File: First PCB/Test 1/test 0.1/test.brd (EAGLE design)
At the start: 62.2 x 39 mm, 7 parts, among them SW2 B3U-1000P

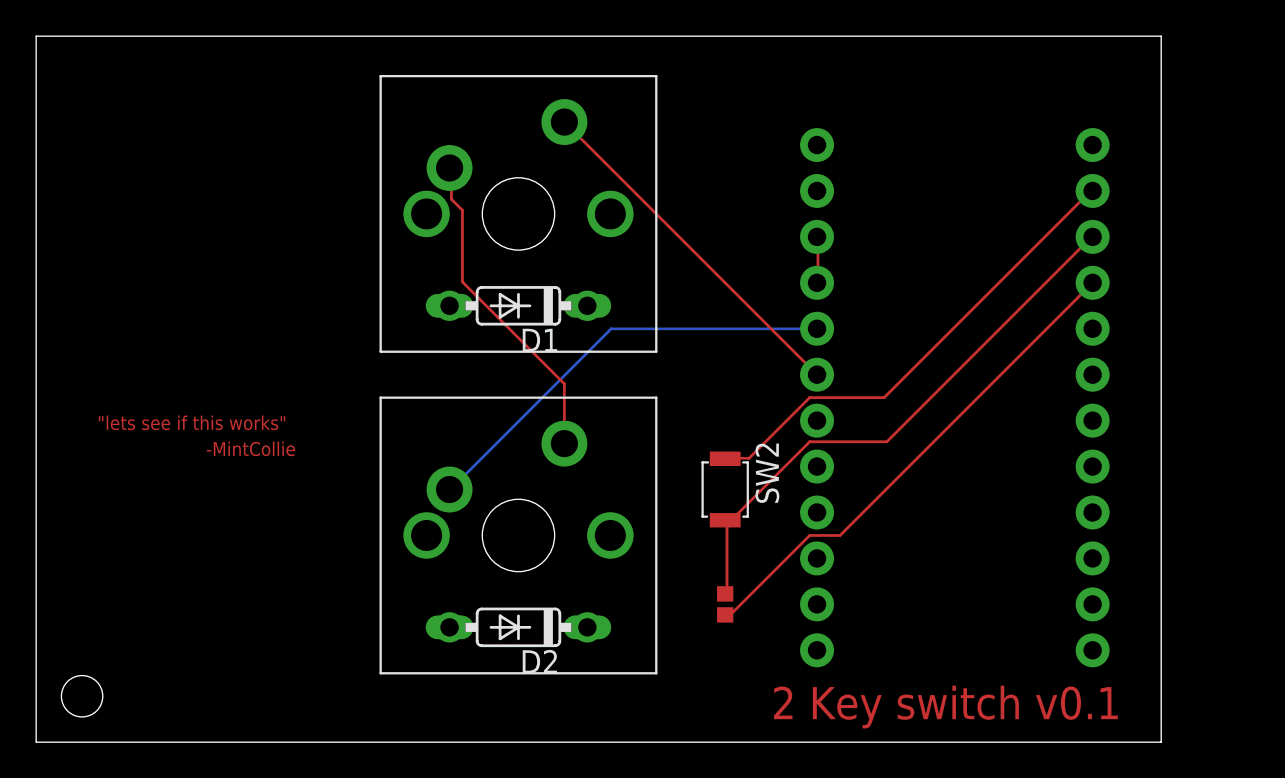
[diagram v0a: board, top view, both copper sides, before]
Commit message: Added QR code to bottom layer, Need to resize. Need to fix diode route and then submit for review
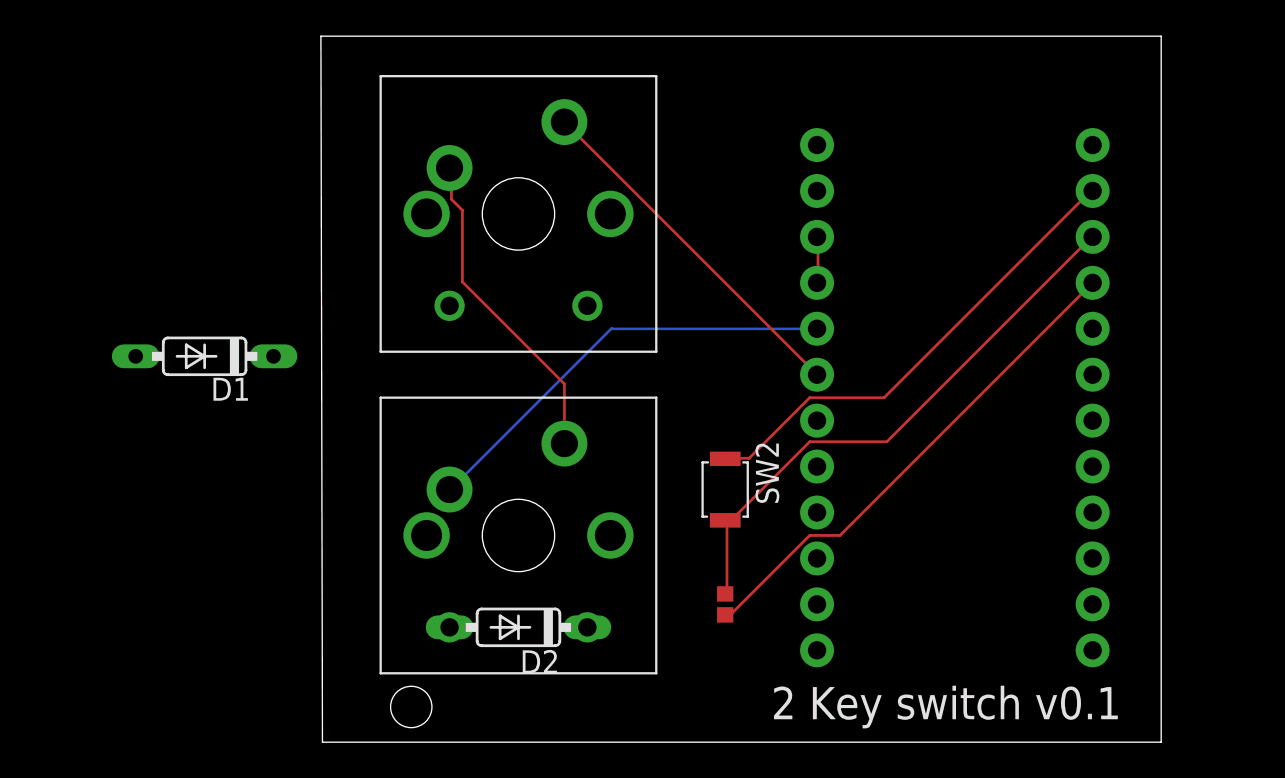
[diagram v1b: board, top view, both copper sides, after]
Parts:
- moved D1 17.6 mm to (71.5, 44.2)
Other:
- board size 62.2 x 39 mm -> 46.5 x 39 mm
- board text added: "C:/Users/Mint/Pictures/test2.bmp"

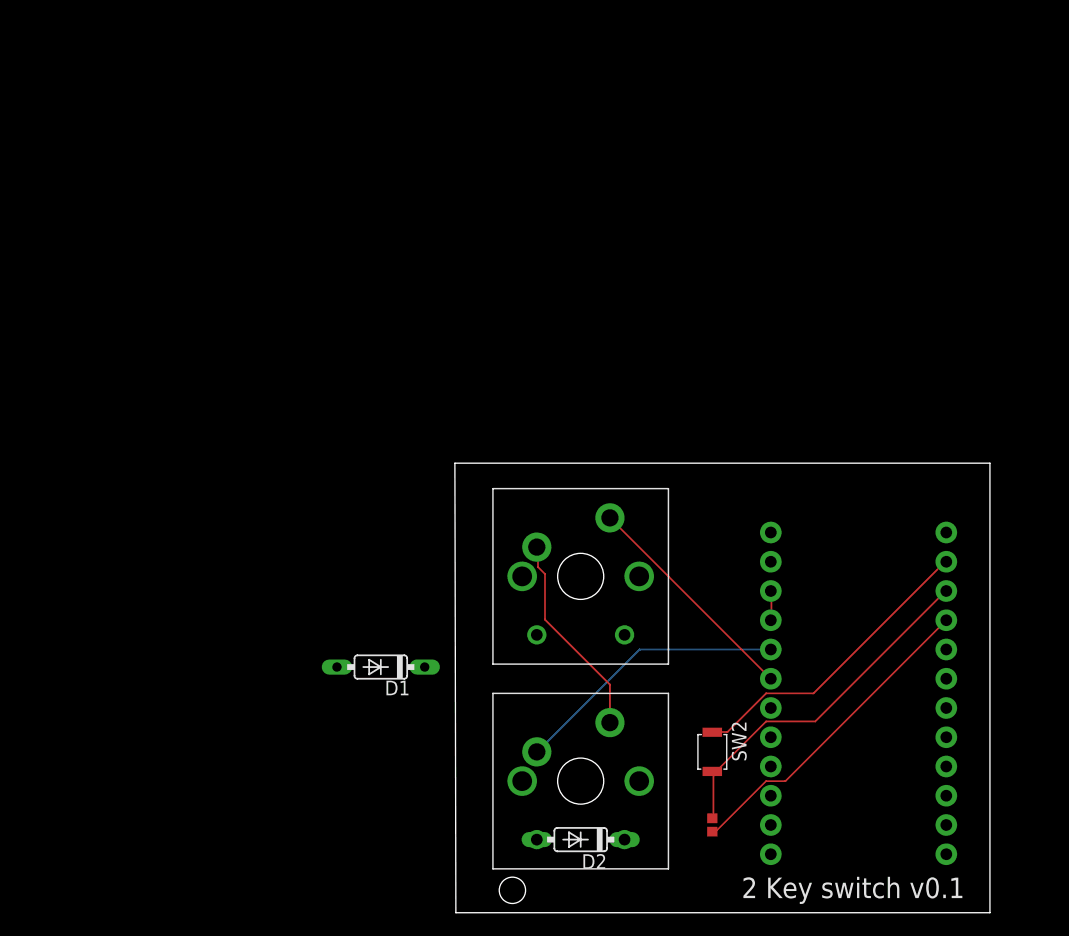
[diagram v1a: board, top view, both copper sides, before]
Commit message: slight changes to board layout need to finish still
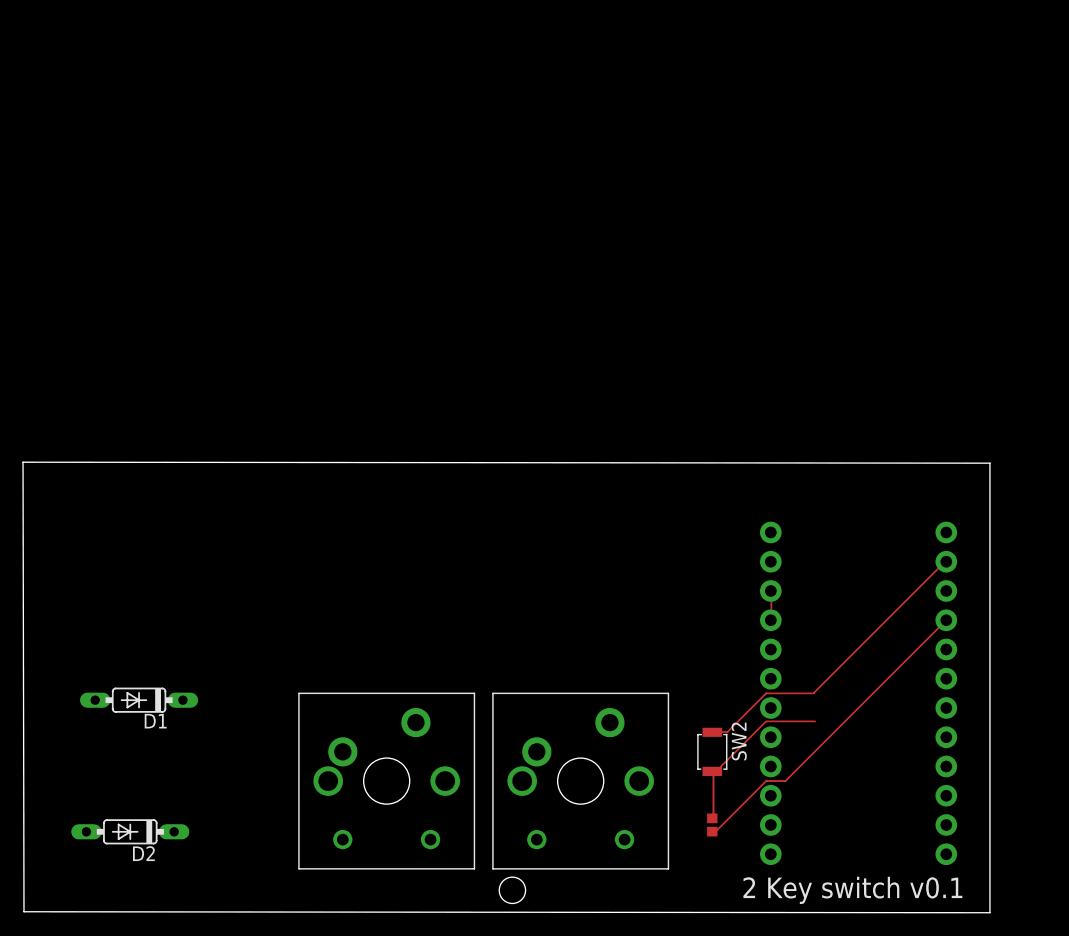
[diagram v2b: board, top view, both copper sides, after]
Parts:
- moved D2 39.1 mm to (49.8, 29.9)
- moved DIODE1 24.5 mm to (72.1, 34.3)
- moved D1 21.2 mm to (50.5, 41.3)
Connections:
- removed net N$10: D1.C, DIODE1.D2
- removed net N$6: B1.6, DIODE1.SW2
- removed net N$8: D2.C, DIODE.D2
- removed net N$9: D1.A, DIODE1.D1
- net N$4: now also B1.6; no longer B1.5
- net N$5: now also D2.C; no longer DIODE.SW2
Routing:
- net N$4: track 24.0 -> 0.11 mm
- net N$6: track 19.8 -> 0.00 mm
- net N$5: track 17.9 -> 0.00 mm
- net N$1: track 31.0 -> 15.0 mm
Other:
- board size 46.5 x 39 mm -> 84 x 39.1 mm
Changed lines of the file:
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@@
 <board>
 <plain>
-<wire x1="78.06108125" y1="22.86" x2="124.44" y2="22.86" width="0" layer="20"/>
+<wire x1="40.5575" y1="22.944659375" x2="124.44" y2="22.86" width="0" layer="20"/>
 <wire x1="124.44" y1="22.86" x2="124.44" y2="61.9" width="0" layer="20"/>
-<wire x1="124.44" y1="61.9" x2="77.976421875" y2="61.900003125" width="0" layer="20"/>
-<wire x1="77.976421875" y1="61.900003125" x2="78.06108125" y2="22.86" width="0" layer="20"/>
+<wire x1="124.44" y1="61.9" x2="40.472840625" y2="61.9846625" width="0" layer="20"/>
+<wire x1="40.472840625" y1="61.9846625" x2="40.5575" y2="22.944659375" width="0" layer="20"/>
 <text x="102.87" y="24.13" size="1.778" layer="25" font="vector">2 Key switch v0.1</text>
 <hole x="82.971509375" y="24.8073875" drill="2.286"/>
@@
 <attribute name="VALUE" x="113.03" y="26.416" size="0.6096" layer="27" font="vector" ratio="20" align="top-center"/>
 </element>
-<element name="D1" library="diode" library_urn="urn:adsk.eagle:library:210" package="DO35-7" package3d_urn="urn:adsk.eagle:package:43339/2" value="1N4148DO35-7" x="71.54506875" y="44.196278125" smashed="yes" rot="R180">
-<attribute name="MF" value="" x="47.41506875" y="100.076278125" size="1.778" layer="27" rot="R180" display="off"/>
-<attribute name="MPN" value="" x="47.41506875" y="100.076278125" size="1.778" layer="27" rot="R180" display="off"/>
-<attribute name="NAME" x="74.08504375" y="43.010934375" size="1.27" layer="25" ratio="10" rot="R180"/>
-<attribute name="OC_NEWARK" value="unknown" x="47.41506875" y="100.076278125" size="1.778" layer="27" rot="R180" display="off"/>
+<element name="D1" library="diode" library_urn="urn:adsk.eagle:library:210" package="DO35-7" package3d_urn="urn:adsk.eagle:package:43339/2" value="1N4148DO35-7" x="50.5498375" y="41.3179" smashed="yes" rot="R180">
+<attribute name="MF" value="" x="26.4198375" y="97.1979" size="1.778" layer="27" rot="R180" display="off"/>
+<attribute name="MPN" value="" x="26.4198375" y="97.1979" size="1.778" layer="27" rot="R180" display="off"/>
+<attribute name="NAME" x="53.0898125" y="40.13255625" size="1.27" layer="25" ratio="10" rot="R180"/>
+<attribute name="OC_NEWARK" value="unknown" x="26.4198375" y="97.1979" size="1.778" layer="27" rot="R180" display="off"/>
 </element>
-<element name="D2" library="diode" library_urn="urn:adsk.eagle:library:210" package="DO35-7" package3d_urn="urn:adsk.eagle:package:43339/2" value="1N4148DO35-7" x="88.9" y="29.21" smashed="yes" rot="R180">
-<attribute name="MF" value="" x="48.26" y="85.09" size="1.778" layer="27" rot="R180" display="off"/>
-<attribute name="MPN" value="" x="48.26" y="85.09" size="1.778" layer="27" rot="R180" display="off"/>
-<attribute name="NAME" x="91.186" y="27.94" size="1.27" layer="25" ratio="10" rot="R180"/>
-<attribute name="OC_NEWARK" value="unknown" x="48.26" y="85.09" size="1.778" layer="27" rot="R180" display="off"/>
+<element name="D2" library="diode" library_urn="urn:adsk.eagle:library:210" package="DO35-7" package3d_urn="urn:adsk.eagle:package:43339/2" value="1N4148DO35-7" x="49.7879125" y="29.887265625" smashed="yes" rot="R180">
+<attribute name="MF" value="" x="9.1479125" y="85.767265625" size="1.778" layer="27" rot="R180" display="off"/>
+<attribute name="MPN" value="" x="9.1479125" y="85.767265625" size="1.778" layer="27" rot="R180" display="off"/>
+<attribute name="NAME" x="52.0739125" y="28.617265625" size="1.27" layer="25" ratio="10" rot="R180"/>
+<attribute name="OC_NEWARK" value="unknown" x="9.1479125" y="85.767265625" size="1.778" layer="27" rot="R180" display="off"/>
 </element>
 <element name="DIODE" library="cherrymx" package="CHERRY-MX-DIODE" value="CHERRY-MX-DIODE" x="88.9" y="34.29" smashed="yes">
@@
 <attribute name="OC_NEWARK" value="unknown" x="129.54" y="25.4" size="1.778" layer="27" display="off"/>
 </element>
-<element name="DIODE1" library="cherrymx" package="CHERRY-MX-DIODE" value="CHERRY-MX-DIODE" x="88.9" y="52.07" smashed="yes">
-<attribute name="MF" value="" x="110.49" y="7.62" size="1.778" layer="27" display="off"/>
-<attribute name="MPN" value="" x="110.49" y="7.62" size="1.778" layer="27" display="off"/>
-<attribute name="OC_NEWARK" value="unknown" x="110.49" y="7.62" size="1.778" layer="27" display="off"/>
+<element name="DIODE1" library="cherrymx" package="CHERRY-MX-DIODE" value="CHERRY-MX-DIODE" x="72.05301875" y="34.291778125" smashed="yes">
+<attribute name="MF" value="" x="93.64301875" y="-10.158221875" size="1.778" layer="27" display="off"/>
+<attribute name="MPN" value="" x="93.64301875" y="-10.158221875" size="1.778" layer="27" display="off"/>
+<attribute name="OC_NEWARK" value="unknown" x="93.64301875" y="-10.158221875" size="1.778" layer="27" display="off"/>
 </element>
 <element name="R1" library="SparkFun-Resistors" package="0402" value="10k" x="100.33" y="30.48" smashed="yes" rot="R90">
@@
 <wire x1="105.0036" y1="39.4716" x2="100.7364" y2="35.2044" width="0.1524" layer="1"/>
 <wire x1="109.2708" y1="39.4716" x2="105.0036" y2="39.4716" width="0.1524" layer="1"/>
-<wire x1="120.5484" y1="50.7492" x2="109.2708" y2="39.4716" width="0.1524" layer="1"/>
 <wire x1="100.4316" y1="35.2044" x2="100.33" y2="35.13" width="0.1524" layer="1"/>
 <wire x1="120.5484" y1="50.7492" x2="120.65" y2="50.8" width="0.1524" layer="1"/>
+<wire x1="109.2708" y1="39.4716" x2="120.5484" y2="50.7492" width="0" layer="19" extent="1-1"/>
 </signal>
 <signal name="N$2">
@@
 <wire x1="120.5484" y1="53.34" x2="120.65" y2="53.34" width="0.1524" layer="1"/>
 </signal>
-<signal name="N$5">
-<contactref element="DIODE1" pad="SW1"/>
-<contactref element="DIODE" pad="SW2"/>
-<wire x1="85.1916" y1="52.8828" x2="85.1916" y2="54.5592" width="0.1524" layer="1"/>
-<wire x1="85.8012" y1="52.2732" x2="85.1916" y2="52.8828" width="0.1524" layer="1"/>
-<wire x1="85.8012" y1="48.3108" x2="85.8012" y2="52.2732" width="0.1524" layer="1"/>
-<wire x1="91.44" y1="42.672" x2="85.8012" y2="48.3108" width="0.1524" layer="1"/>
-<wire x1="91.44" y1="39.37" x2="91.44" y2="42.672" width="0.1524" layer="1"/>
-<wire x1="85.1916" y1="54.5592" x2="85.09" y2="54.61" width="0.1524" layer="1"/>
-</signal>
-<signal name="N$6">
-<contactref element="DIODE1" pad="SW2"/>
+<signal name="N$4">
+<contactref element="DIODE" pad="SW1"/>
+<wire x1="85.1916" y1="36.8808" x2="85.09" y2="36.83" width="0.1524" layer="16"/>
 <contactref element="B1" pad="6"/>
-<wire x1="91.44" y1="57.15" x2="105.41" y2="43.18" width="0.1524" layer="1"/>
-</signal>
-<signal name="N$4">
-<contactref element="B1" pad="5"/>
-<contactref element="DIODE" pad="SW1"/>
-<wire x1="94.0308" y1="45.72" x2="105.41" y2="45.72" width="0.1524" layer="16"/>
-<wire x1="85.1916" y1="36.8808" x2="94.0308" y2="45.72" width="0.1524" layer="16"/>
-<wire x1="85.1916" y1="36.8808" x2="85.09" y2="36.83" width="0.1524" layer="16"/>
+<wire x1="85.1916" y1="36.8808" x2="105.41" y2="43.18" width="0" layer="19" extent="16-16"/>
 </signal>
 <signal name="N$7">
@@
 <contactref element="D2" pad="A"/>
 </signal>
-<signal name="N$8">
+<signal name="N$5">
 <contactref element="D2" pad="C"/>
-<contactref element="DIODE" pad="D2"/>
-</signal>
-<signal name="N$9">
-<contactref element="DIODE1" pad="D1"/>
-<contactref element="D1" pad="A"/>
-</signal>
-<signal name="N$10">
-<contactref element="DIODE1" pad="D2"/>
-<contactref element="D1" pad="C"/>
+<contactref element="DIODE1" pad="SW1"/>
+<wire x1="53.5979125" y1="29.887265625" x2="68.24301875" y2="36.831778125" width="0" layer="19" extent="1-1"/>
 </signal>
 </signals>

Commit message: finished board and submitted for review, https://geekhack.org/index.php?topic=102077.0
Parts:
- removed DIODE, DIODE1: CHERRY-MX-DIODE, cherrymx:CHERRY-MX-DIODE
- added D3, D4: 1N4148DO35-7, diode:DO35-7
- added U$1, U$2, U$3, U$4: CHERRY-MX, cherrymx:CHERRY-MX
- moved R1 66.1 mm to (96.5, 96.5), turned to 180 degrees
- moved D2 66.0 mm to (92.7, 80.0), turned to 0 degrees
- moved SW2 61.0 mm to (87.6, 96.5), turned to 0 degrees
- moved D1 45.7 mm to (74.9, 80.0), turned to 0 degrees
- moved B1 34.3 mm to (111.8, 77.5)
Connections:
- new net N$10: D4.A, U$2.SW2
- new net N$12: D3.A, U$3.SW2
- new net N$6: B1.7, U$1.SW1, U$2.SW1
- new net N$8: D2.A, U$4.SW2
- new net N$9: B1.8, U$3.SW1, U$4.SW1
- net N$4: now also B1.5, D1.C, D2.C; no longer B1.6, DIODE.SW1
- net N$5: now also D1.A, U$1.SW2; no longer D2.C, DIODE1.SW1
- net N$7: now also B1.6, D3.C, D4.C; no longer D2.A, DIODE.D1
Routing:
- net N$7: track 0.00 -> 42.9 mm
- net N$9: track 0.00 -> 40.5 mm
- net N$4: track 0.11 -> 34.5 mm
- net N$6: track 0.00 -> 33.9 mm
- net N$12: track 0.00 -> 27.7 mm
- net N$1: track 15.0 -> 35.5 mm
- net N$3: track 26.4 -> 38.1 mm
- net N$8: track 0.00 -> 10.7 mm
- net N$10: track 0.00 -> 10.7 mm
- net N$5: track 0.00 -> 6.41 mm
- net GND: track 2.58 -> 0.00 mm
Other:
- board size 84 x 39.1 mm -> 58.4 x 42.9 mm
- board text removed: ""lets see if this works""
- board text removed: "-MintCollie"
- board text removed: "2 Key switch v0.1"
- board text removed: "C:/Users/Mint/Pictures/test2.bmp"
